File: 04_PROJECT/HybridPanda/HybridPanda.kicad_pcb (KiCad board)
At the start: 4 copper layers, 50.5 x 46.7 mm, 123 parts, among them J1 SWD, P1 TYPE-C-31-M-04, Q1 DDTA143ECA-7-F P08, Q2 DDTA143ECA-7-F P08, Q3 PDTC114EU, Q4 HY12P03C2, SW1 SW_Push, U1 AP22615AWU-7, U10 TJA1042TK-3, U11 TJA1042TK-3, U12 XL1509-3.3, U3 10_0_QHHTZB6_3, U5 FM-B1921RGBA-SH, U6 TPS5450DDAR, U7 STM32H725ZGT6, U8 TJA1042TK-3, U9 TJA1042TK-3, Y1 25MHz X322525MOB4SI

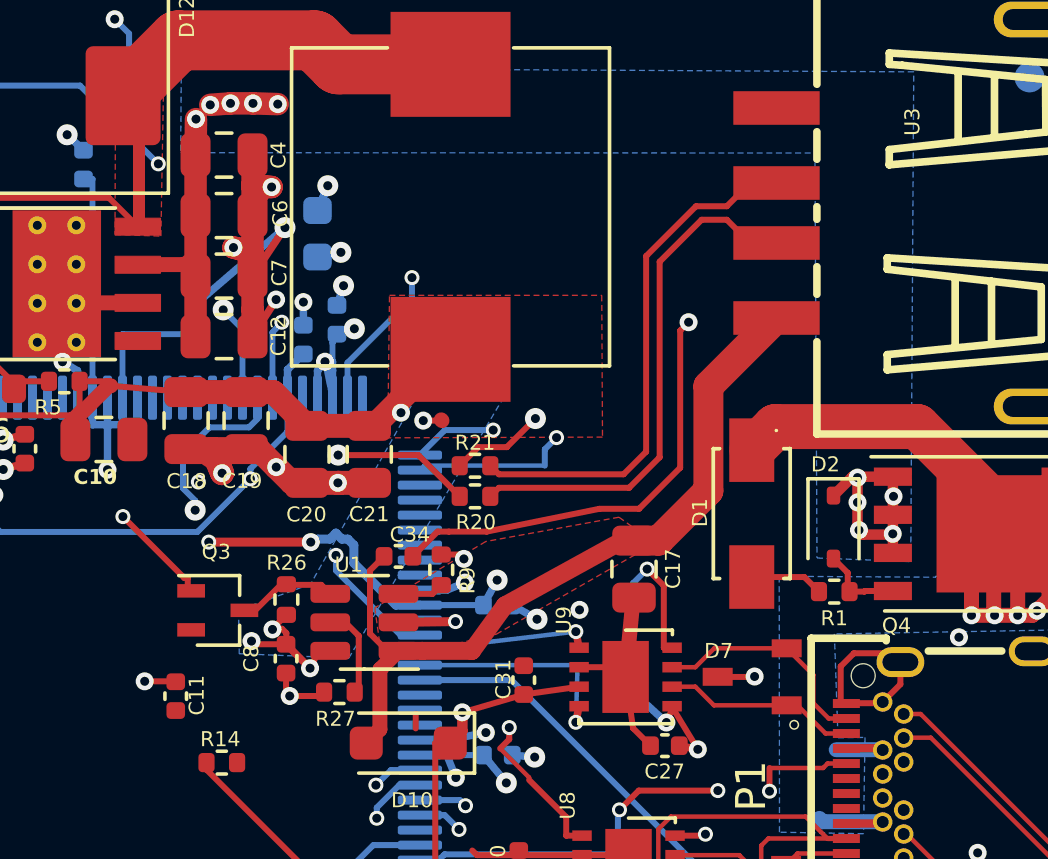
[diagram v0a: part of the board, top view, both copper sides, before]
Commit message: pcb: step 3 WIP - SI/PI HIGH items on schematic and PCB (DRC 0/0)
Schematic: R1 10k 0603, D15 BZT52C12 Vgs clamp, C4/C12 10uF, U13 USBLC6-2SC6.
PCB: R1/D15 rebuilt around the Q4 gate, R20/R21 moved next to U7 pads 100/101,
coupled In1 USB pair to U13 at U3, +5V feed to U1 widened. DRC: 0 clearance,
0 unconnected, 180 total (+1 silk_over_copper). See 06_REPORTS/corr/RESUME_STEP3.md.

Co-authored-by: Copilot <223556219+Copilot@users.noreply.github.com>
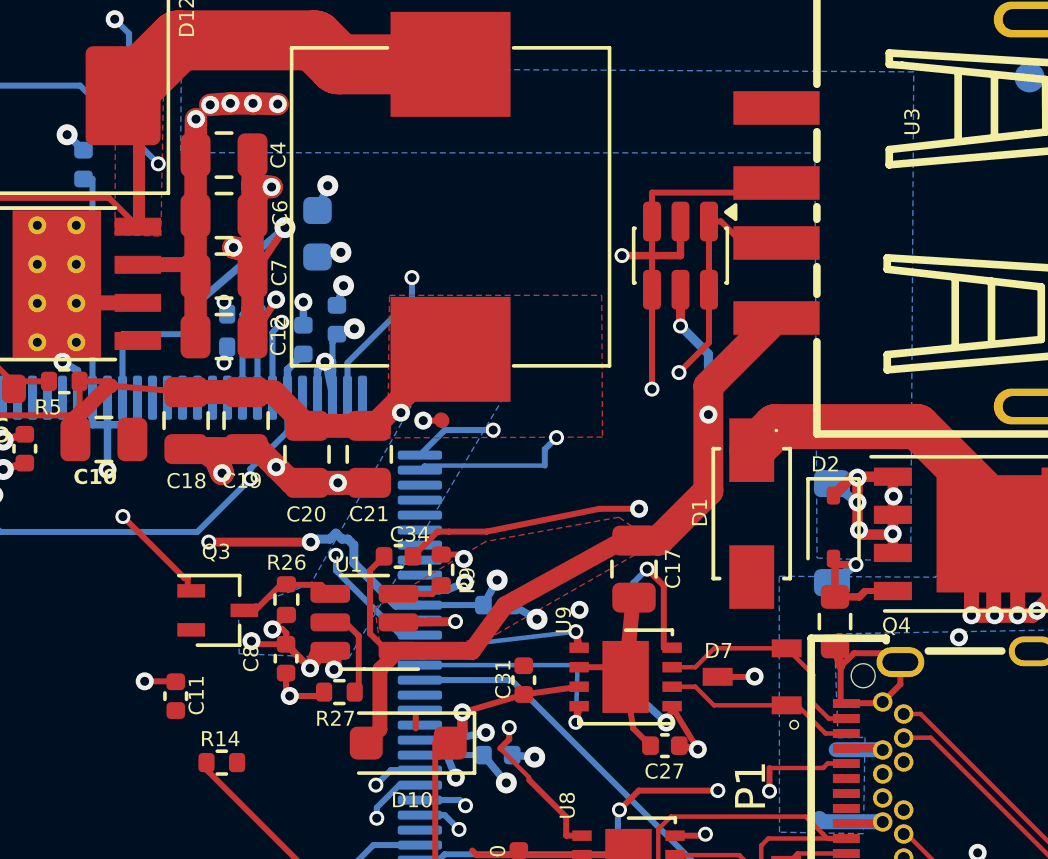
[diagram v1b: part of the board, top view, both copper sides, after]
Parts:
- added D15: BZT52C12, Diode_SMD:D_SOD-123, B.Cu at (133.9, 50.5)
- added U13: USBLC6-2SC6, Package_TO_SOT_SMD:SOT-23-6, F.Cu at (128.8, 41.2)
- C12, C4: value 2.2uF -> 10uF
- R1: value 1K -> 10k; footprint Resistor_SMD:R_0402_1005Metric -> Resistor_SMD:R_0603_1608Metric
- R20, R21: moved to B.Cu
- moved R20 9.85 mm to (114.2, 43.1), turned to 180 degrees
- moved R21 8.70 mm to (114.2, 44.2), turned to 0 degrees
- moved R1 1.00 mm to (134.0, 53.4), turned to 90 degrees
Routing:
- net USB_D+: track 21.5 -> 1.69 mm, vias 2 -> 0
- net USB_D-: track 19.4 -> 3.30 mm, vias 3 -> 0
- net USB_R_D+: track 17.5 -> 25.2 mm, vias 0 -> 2
- net USB_R_D-: track 17.5 -> 24.2 mm, vias 0 -> 2
- net GND: track 223.3 -> 217.7 mm, vias 74 -> 75
- net USB_PWR: track 26.5 -> 31.1 mm, vias 0 -> 2
- net Net-(D15-A): track 2.77 -> 4.91 mm, vias 0 -> 1
- net 12V_Protected: track 70.7 -> 72.7 mm
- net +5V: track 130.7 -> 131.3 mm, vias 14 -> 15

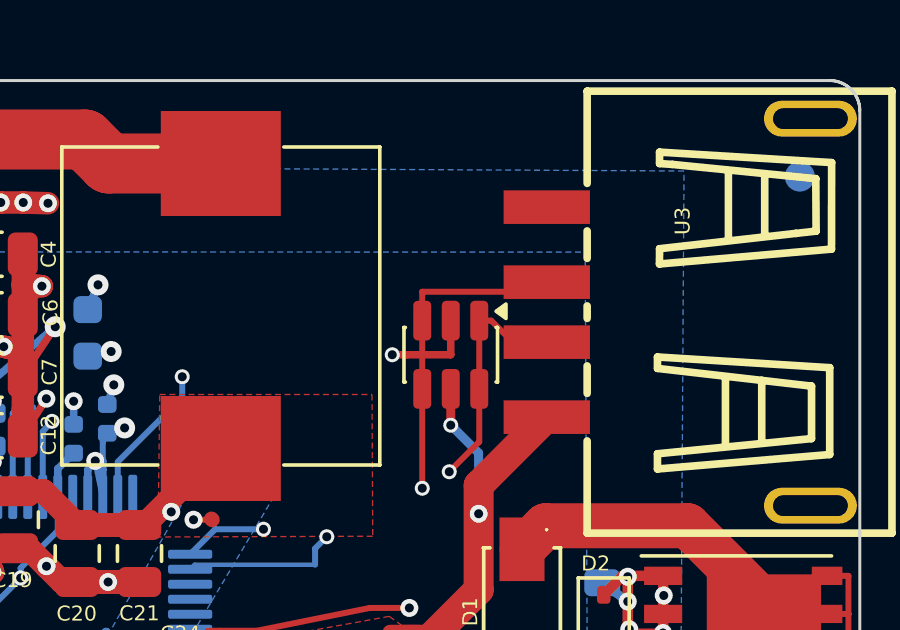
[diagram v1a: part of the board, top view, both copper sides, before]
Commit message: pcb: step 3 - SI/PI HIGH items closed (C4/C12 0805 parity, U13 GND crossing fix, item 16 deferred)
Co-authored-by: Copilot <223556219+Copilot@users.noreply.github.com>
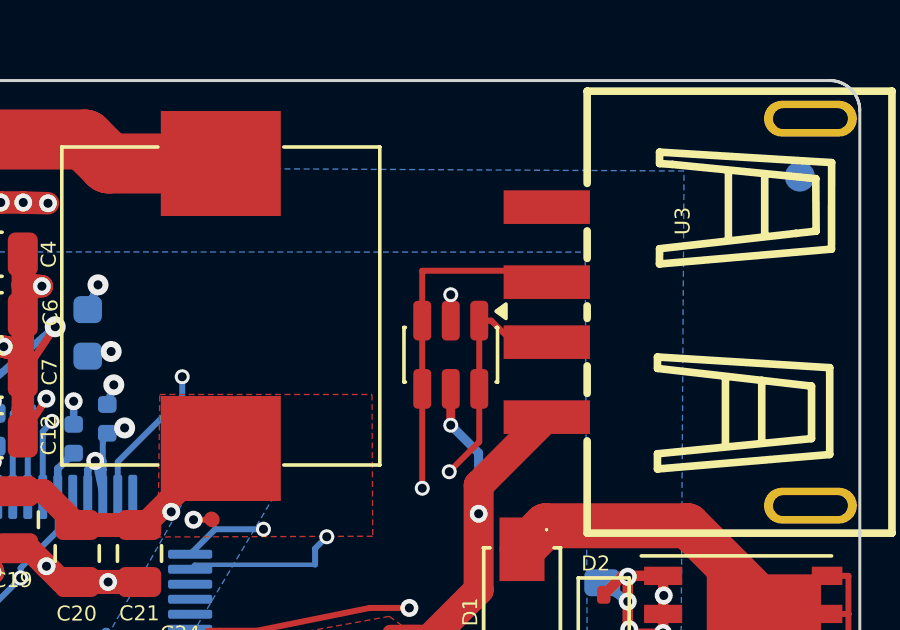
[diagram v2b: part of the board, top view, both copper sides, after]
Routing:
- net GND: track 217.7 -> 215.5 mm
- net USB_R_D+: track 25.2 -> 26.0 mm
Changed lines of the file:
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@@
 	)
 	(segment
-		(start 128.85 41.2)
-		(end 127.4 41.2)
-		(width 0.25)
-		(layer "F.Cu")
-		(net "GND")
-	)
-	(segment
 		(start 101.16 56.19)
 		(end 101.16 57.01)
@@
 	)
 	(segment
-		(start 127.4 41.2)
-		(end 126.9 41.2)
-		(width 0.25)
-		(layer "F.Cu")
-		(net "GND")
-	)
-	(segment
 		(start 110.76 42.775)
 		(end 108.695 42.775)
@@
 	)
 	(segment
-		(start 128.85 40.0625)
-		(end 128.85 41.2)
-		(width 0.25)
-		(layer "F.Cu")
-		(net "GND")
-	)
-	(segment
 		(start 134.190013 62.865506)
 		(end 134.190013 61.820214)
@@
 	)
 	(segment
+		(start 128.85 40.0625)
+		(end 128.85 39.2)
+		(width 0.25)
+		(layer "F.Cu")
+		(net "GND")
+	)
+	(segment
 		(start 126.15 49.64)
 		(end 127.47 49.64)
@@
 	)
 	(via
-		(at 126.9 41.2)
-		(size 0.5)
-		(drill 0.3)
-		(layers "F.Cu" "B.Cu")
-		(net "GND")
-	)
-	(via
 		(at 100.912516 71.07468)
 		(size 0.7)
@@
 	)
 	(via
+		(at 128.85 39.2)
+		(size 0.5)
+		(drill 0.3)
+		(layers "F.Cu" "B.Cu")
+		(net "GND")
+	)
+	(via
 		(at 95.26 42.53)
 		(size 0.6)
@@
 	(segment
 		(start 127.9 40.0625)
-		(end 127.9 39.1)
+		(end 127.9 42.3375)
 		(width 0.2)
 		(layer "F.Cu")
@@
 	(segment
 		(start 127.9 40.0625)
-		(end 127.9 42.3375)
+		(end 127.9 38.4)
 		(width 0.2)
 		(layer "F.Cu")
@@
 	)
 	(segment
-		(start 127.9 45.65)
-		(end 127.9 42.3375)
+		(start 127.9 38.4)
+		(end 130.9 38.4)
 		(width 0.2)
 		(layer "F.Cu")
@@
 	)
 	(segment
-		(start 127.9 39.1)
-		(end 130.75 39.1)
+		(start 127.9 45.65)
+		(end 127.9 42.3375)
 		(width 0.2)
 		(layer "F.Cu")

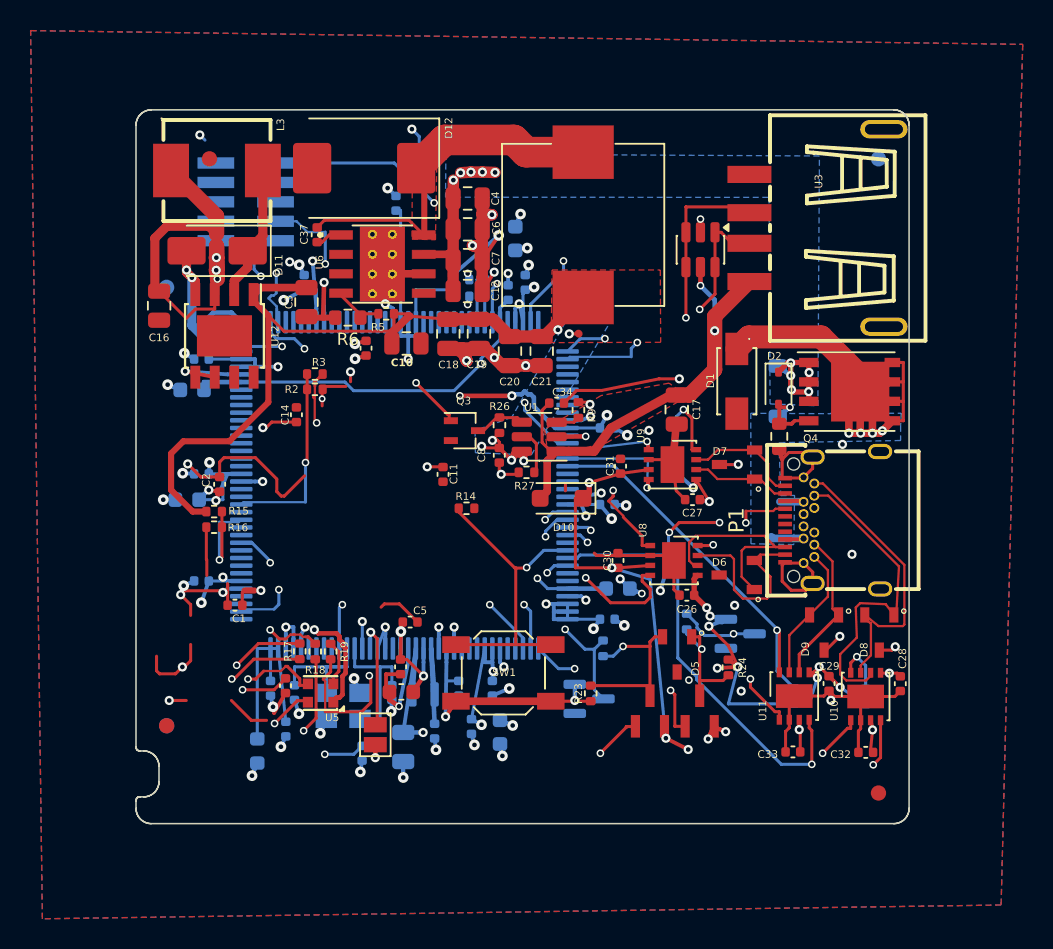
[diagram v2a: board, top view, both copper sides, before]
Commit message: pcb: step 5 - SI/PI MEDIUM items (CAN 0.25, GND zone thermals, vias 0.6, stitching, outline +0.4, C23/C24 18pF, U3 shell GND)
Applied items 24, 26 (partial), 28, 30, 31, 33a/33b, 35 (partial), 12/13/14 (partial),
17 (partial), 20; each change gated by kicad-cli DRC (06_REPORTS/corr/drc_step5*.json).
DRC: 135 total, 0 clearance, 0 unconnected, 0 parity. ERC: 0 errors.
Deferred: 9, 16, 21-23, 25, 27, 29, 32, 34, 36 (see 06_REPORTS/corr/RESUME_STEP3.md).
final_audit.py: BOM MPN finding now data-driven; os._exit avoids pcbnew teardown hang.

Co-authored-by: Copilot <223556219+Copilot@users.noreply.github.com>
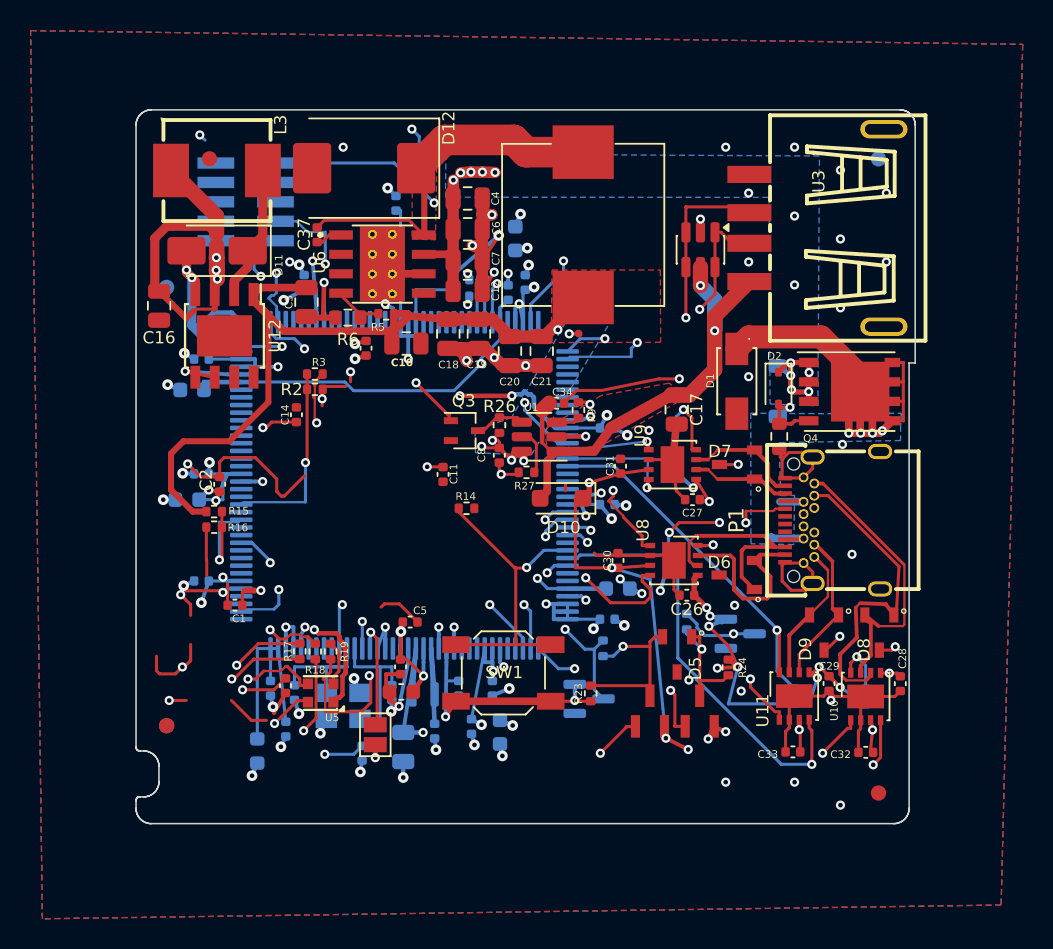
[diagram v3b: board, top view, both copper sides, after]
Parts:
- C23, C24: value 15pF -> 18pF
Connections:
- U3 pad 5: unconnected-(U3-Pad5) -> GND
- U3 pad 6: unconnected-(U3-Pad6) -> GND
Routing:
- net 12V_Protected: track 72.7 -> 48.2 mm
- net +12V: track 42.8 -> 34.2 mm
- net GND: vias 75 -> 91
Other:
- board size 50.5 x 46.7 mm -> 50.9 x 46.7 mm

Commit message: pcb: final - item 15 U6 thermal vias, final DRC/ERC reports, fabrication exports, CORRECOES_APLICADAS and docs
- Item 15: 5 GND thermal vias 0.6/0.3 in the U6 (TPS5450) exposed pad, solid zone
  connection; lower row dropped (SWDIO on In2.Cu underneath).
- final_audit.py: same-net vias inside exposed pads >= 2 mm reported as thermal
  vias (INFO) instead of via-in-pad; BOM MPN finding now data-driven.
- step8_fabricate.py: LEIA-ME BOM/DRC lines derived from data; exports regenerated
  in 07_FABRICATION (BOM_JLC.csv now carries LCSC/MPN from the schematic).
- Final numbers: DRC 135 (0 clearance / 0 unconnected / 0 parity), ERC 0 errors,
  final_audit shorts 0 / via-in-pad 0, step7 no failures.
- Docs: 06_REPORTS/CORRECOES_APLICADAS.md (item -> status -> commit -> evidence,
  deferred list, unverified list), DECISIONS D-34..D-38, PROGRESS, RELATORIO_FINAL 1.1.

Co-authored-by: Copilot <223556219+Copilot@users.noreply.github.com>
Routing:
- net GND: vias 91 -> 96
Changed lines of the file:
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@@
+	)
+	(via
+		(at 108.06 41.2)
+		(size 0.6)
+		(drill 0.3)
+		(layers "F.Cu" "B.Cu")
+		(net "GND")
 	)
 	(via
@@
 	)
 	(via
+		(at 108.71 40.84)
+		(size 0.6)
+		(drill 0.3)
+		(layers "F.Cu" "B.Cu")
+		(net "GND")
+	)
+	(via
 		(at 102.0036 41.9991)
 		(size 0.6)
@@
 	)
 	(via
+		(at 108.71 42.14)
+		(size 0.6)
+		(drill 0.3)
+		(layers "F.Cu" "B.Cu")
+		(net "GND")
+	)
+	(via
 		(at 132 37.5)
 		(size 0.6)
@@
 	)
 	(via
+		(at 107.41 42.14)
+		(size 0.6)
+		(drill 0.3)
+		(layers "F.Cu" "B.Cu")
+		(net "GND")
+	)
+	(via
 		(at 108.639218 71.374072)
 		(size 0.7)
@@
 		(size 0.6)
 		(drill 0.3)
+		(layers "F.Cu" "B.Cu")
+		(net "GND")
+	)
+	(via
+		(at 107.41 40.84)
+		(size 0.6)
+		(drill 0.3)
